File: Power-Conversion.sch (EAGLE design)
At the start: 46 parts, among them Q1 SUM90P10-19L, U7 LM2678

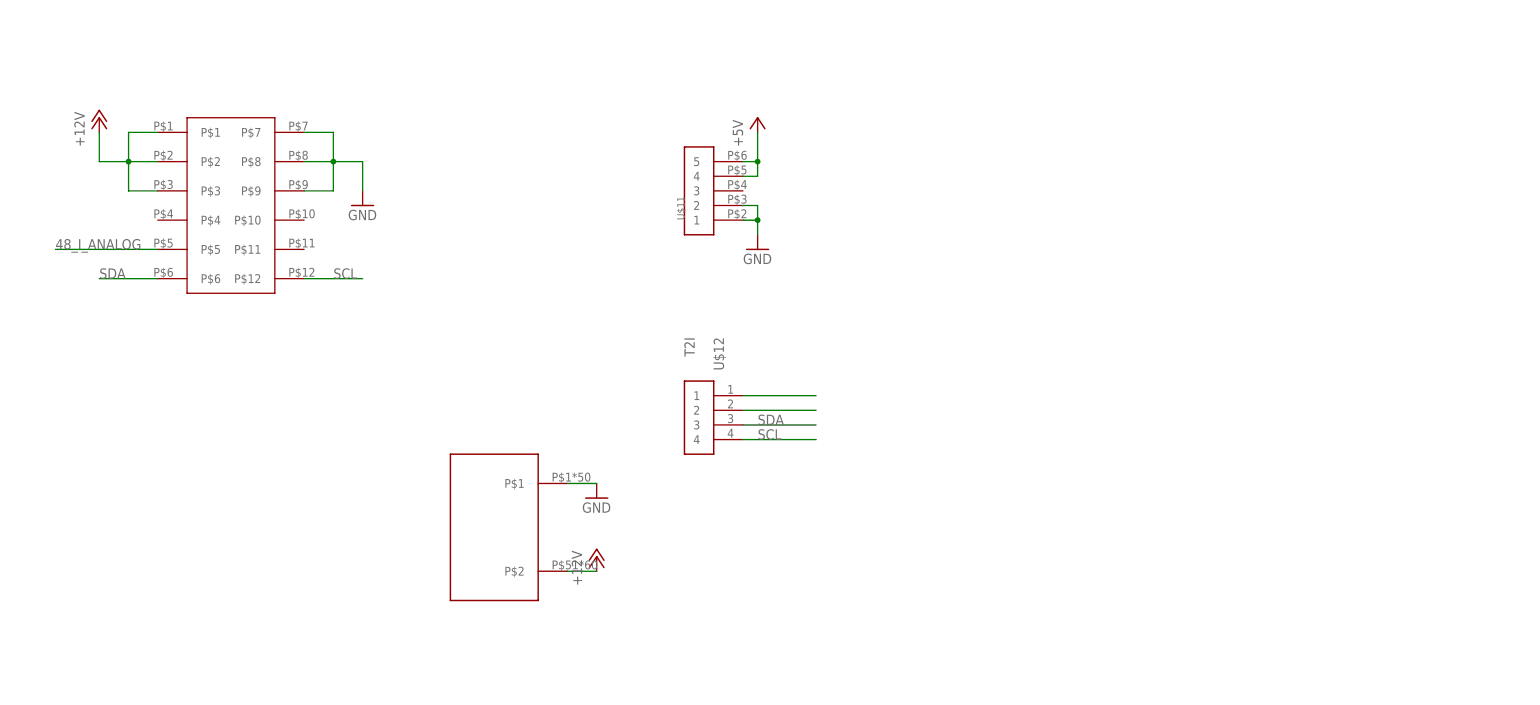
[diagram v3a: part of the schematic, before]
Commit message: Added new ESC to power distribution board part
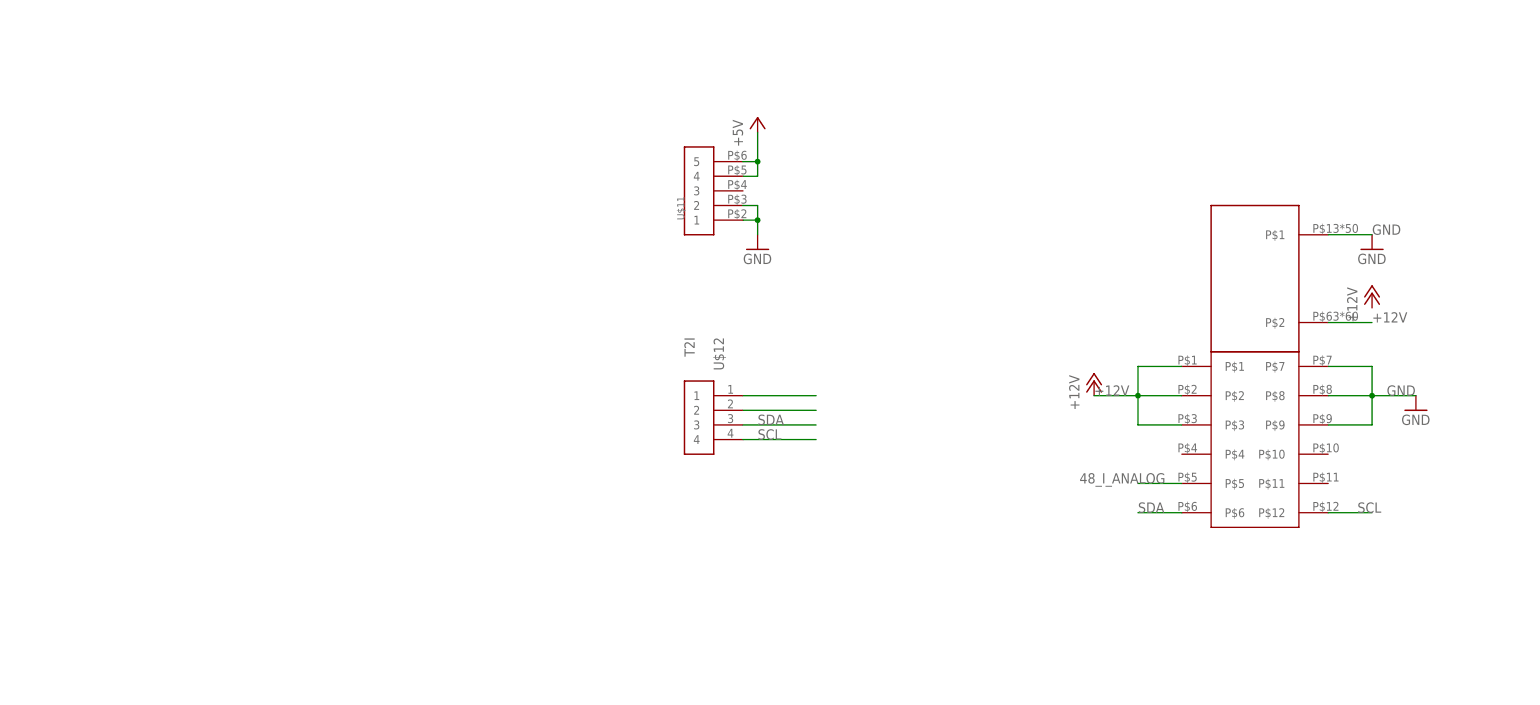
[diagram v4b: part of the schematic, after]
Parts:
- removed U$16: POWER_BRICK_CONNECTORS(2X6), MotherBoardParts2:POWER_BRICK_CONNECTORS(2X6)
- removed U$17: ESC-CONNECTORPARALLELL, MotherboardParts:ESC-CONNECTORPARALLELL
- added U$3: ESC-FULL, MotherboardParts:ESC-FULL
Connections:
- net +12V: now also U$3G$1.P$2, U$3G$2.P$1, U$3G$2.P$2, U$3G$2.P$3; no longer U$16.P$1, U$16.P$2, U$16.P$3, U$17.P$2
- net 48_I_ANALOG: now also U$3G$2.P$5; no longer U$16.P$5
- net GND: now also U$3G$1.P$1, U$3G$2.P$7, U$3G$2.P$8, U$3G$2.P$9; no longer U$16.P$7, U$16.P$8, U$16.P$9, U$17.P$1
- net SCL: now also U$3G$2.P$12; no longer U$16.P$12
- net SDA: now also U$3G$2.P$6; no longer U$16.P$6
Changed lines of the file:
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@@
 <?xml version="1.0" encoding="utf-8"?>
 <!DOCTYPE eagle SYSTEM "eagle.dtd">
-<eagle version="8.3.2">
+<eagle version="8.5.0">
 <drawing>
 <settings>
@@
 <part name="J1" library="SparkFun-Connectors" deviceset="BANANA_CONN" device=""/>
 <part name="J2" library="SparkFun-Connectors" deviceset="BANANA_CONN" device=""/>
-<part name="U$16" library="MotherBoardParts2" deviceset="POWER_BRICK_CONNECTORS(2X6)" device=""/>
 <part name="GND6" library="supply1" deviceset="GND" device=""/>
 <part name="U$2" library="diode" deviceset="DIODE" device=""/>
@@
 <part name="F7" library="PowerComponents" deviceset="PTC(2920L)" device="" value="10A"/>
 <part name="P+18" library="supply1" deviceset="+12V" device=""/>
-<part name="U$17" library="MotherboardParts" deviceset="ESC-CONNECTOR" device="PARALLELL" value="ESC-CONNECTORPARALLELL"/>
+<part name="U$3" library="MotherboardParts" deviceset="ESC-FULL" device=""/>
 </parts>
 <sheets>
@@
 <instance part="J1" gate="G$1" x="33.02" y="104.14"/>
 <instance part="J2" gate="G$1" x="33.02" y="99.06"/>
-<instance part="U$16" gate="G$1" x="50.8" y="378.46"/>
-<instance part="GND6" gate="1" x="73.66" y="373.38"/>
+<instance part="GND6" gate="1" x="248.92" y="365.76"/>
 <instance part="U$2" gate="G$1" x="53.34" y="447.04"/>
 <instance part="U$18" gate="G$1" x="142.24" y="441.96"/>
 <instance part="U$19" gate="G$1" x="233.68" y="441.96"/>
-<instance part="GND5" gate="1" x="114.3" y="322.58"/>
+<instance part="GND5" gate="1" x="256.54" y="337.82"/>
 <instance part="U$20" gate="G$1" x="50.8" y="482.6"/>
 <instance part="U$21" gate="G$1" x="139.7" y="482.6"/>
@@
 <instance part="P+9" gate="1" x="233.68" y="462.28"/>
 <instance part="P+13" gate="1" x="320.04" y="462.28"/>
-<instance part="P+14" gate="1" x="27.94" y="388.62"/>
-<instance part="P+15" gate="1" x="114.3" y="312.42"/>
+<instance part="P+14" gate="1" x="200.66" y="342.9"/>
+<instance part="P+15" gate="1" x="248.92" y="358.14"/>
 <instance part="R15" gate="G$1" x="187.96" y="520.7" rot="R180"/>
 <instance part="R5" gate="G$1" x="187.96" y="510.54" rot="R180"/>
@@
 <instance part="F7" gate="G$1" x="246.38" y="238.76" rot="MR90"/>
 <instance part="P+18" gate="1" x="246.38" y="251.46"/>
-<instance part="U$17" gate="G$1" x="96.52" y="317.5"/>
+<instance part="U$3" gate="G$1" x="228.6" y="360.68"/>
+<instance part="U$3" gate="G$2" x="226.06" y="327.66"/>
 </instances>
 <busses>
@@
 </segment>
 <segment>
-<pinref part="U$16" gate="G$1" pin="P$7"/>
-<wire x1="63.5" y1="386.08" x2="68.58" y2="386.08" width="0.1524" layer="91"/>
-<wire x1="68.58" y1="386.08" x2="68.58" y2="381" width="0.1524" layer="91"/>
-<pinref part="U$16" gate="G$1" pin="P$8"/>
-<wire x1="68.58" y1="381" x2="63.5" y2="381" width="0.1524" layer="91"/>
-<pinref part="U$16" gate="G$1" pin="P$9"/>
-<wire x1="63.5" y1="375.92" x2="68.58" y2="375.92" width="0.1524" layer="91"/>
-<wire x1="68.58" y1="375.92" x2="68.58" y2="381" width="0.1524" layer="91"/>
-<junction x="68.58" y="381"/>
-<wire x1="68.58" y1="381" x2="73.66" y2="381" width="0.1524" layer="91"/>
-<wire x1="73.66" y1="381" x2="73.66" y2="375.92" width="0.1524" layer="91"/>
-<pinref part="GND6" gate="1" pin="GND"/>
-</segment>
-<segment>
 <pinref part="U$20" gate="G$1" pin="D_GND"/>
 <wire x1="68.58" y1="472.44" x2="73.66" y2="472.44" width="0.1524" layer="91"/>
@@
 </segment>
 <segment>
-<pinref part="U$17" gate="G$1" pin="P$1"/>
-<wire x1="109.22" y1="325.12" x2="114.3" y2="325.12" width="0.1524" layer="91"/>
+<pinref part="U$3" gate="G$1" pin="P$1"/>
+<wire x1="241.3" y1="368.3" x2="248.92" y2="368.3" width="0.1524" layer="91"/>
+<label x="248.92" y="368.3" size="1.778" layer="95"/>
+<pinref part="GND6" gate="1" pin="GND"/>
+</segment>
+<segment>
+<pinref part="U$3" gate="G$2" pin="P$7"/>
+<wire x1="241.3" y1="345.44" x2="248.92" y2="345.44" width="0.1524" layer="91"/>
+<pinref part="U$3" gate="G$2" pin="P$9"/>
+<wire x1="241.3" y1="335.28" x2="248.92" y2="335.28" width="0.1524" layer="91"/>
+<wire x1="248.92" y1="345.44" x2="248.92" y2="340.36" width="0.1524" layer="91"/>
+<pinref part="U$3" gate="G$2" pin="P$8"/>
+<wire x1="248.92" y1="340.36" x2="248.92" y2="335.28" width="0.1524" layer="91"/>
+<wire x1="241.3" y1="340.36" x2="248.92" y2="340.36" width="0.1524" layer="91"/>
+<junction x="248.92" y="340.36"/>
+<wire x1="248.92" y1="340.36" x2="256.54" y2="340.36" width="0.1524" layer="91"/>
+<label x="251.46" y="340.36" size="1.778" layer="95"/>
 <pinref part="GND5" gate="1" pin="GND"/>
 </segment>
@@
 </segment>
 <segment>
-<pinref part="U$16" gate="G$1" pin="P$1"/>
-<wire x1="38.1" y1="386.08" x2="33.02" y2="386.08" width="0.1524" layer="91"/>
-<pinref part="U$16" gate="G$1" pin="P$2"/>
-<wire x1="33.02" y1="386.08" x2="33.02" y2="381" width="0.1524" layer="91"/>
-<wire x1="33.02" y1="381" x2="38.1" y2="381" width="0.1524" layer="91"/>
-<pinref part="U$16" gate="G$1" pin="P$3"/>
-<wire x1="38.1" y1="375.92" x2="33.02" y2="375.92" width="0.1524" layer="91"/>
-<wire x1="33.02" y1="375.92" x2="33.02" y2="381" width="0.1524" layer="91"/>
-<junction x="33.02" y="381"/>
-<wire x1="33.02" y1="381" x2="27.94" y2="381" width="0.1524" layer="91"/>
-<wire x1="27.94" y1="381" x2="27.94" y2="386.08" width="0.1524" layer="91"/>
-<pinref part="P+14" gate="1" pin="+12V"/>
-</segment>
-<segment>
 <pinref part="F7" gate="G$1" pin="2"/>
 <pinref part="P+18" gate="1" pin="+12V"/>
@@
 </segment>
 <segment>
-<pinref part="U$17" gate="G$1" pin="P$2"/>
-<wire x1="109.22" y1="309.88" x2="114.3" y2="309.88" width="0.1524" layer="91"/>
-<pinref part="P+15" gate="1" pin="+12V"/>
+<pinref part="U$3" gate="G$1" pin="P$2"/>
+<wire x1="241.3" y1="353.06" x2="248.92" y2="353.06" width="0.1524" layer="91"/>
+<label x="248.92" y="353.06" size="1.778" layer="95"/>
+</segment>
+<segment>
+<pinref part="U$3" gate="G$2" pin="P$1"/>
+<wire x1="215.9" y1="345.44" x2="208.28" y2="345.44" width="0.1524" layer="91"/>
+<pinref part="U$3" gate="G$2" pin="P$3"/>
+<wire x1="215.9" y1="335.28" x2="208.28" y2="335.28" width="0.1524" layer="91"/>
+<wire x1="208.28" y1="345.44" x2="208.28" y2="340.36" width="0.1524" layer="91"/>
+<pinref part="U$3" gate="G$2" pin="P$2"/>
+<wire x1="208.28" y1="340.36" x2="208.28" y2="335.28" width="0.1524" layer="91"/>
+<wire x1="215.9" y1="340.36" x2="208.28" y2="340.36" width="0.1524" layer="91"/>
+<junction x="208.28" y="340.36"/>
+<wire x1="208.28" y1="340.36" x2="200.66" y2="340.36" width="0.1524" layer="91"/>
+<label x="200.66" y="340.36" size="1.778" layer="95"/>
+<pinref part="P+14" gate="1" pin="+12V"/>
 </segment>
 </net>
@@
 <net name="SCL" class="0">
 <segment>
-<pinref part="U$16" gate="G$1" pin="P$12"/>
-<wire x1="63.5" y1="360.68" x2="73.66" y2="360.68" width="0.1524" layer="91"/>
-<label x="68.58" y="360.68" size="1.778" layer="95"/>
-</segment>
-<segment>
 <pinref part="R5" gate="G$1" pin="2"/>
 <wire x1="182.88" y1="510.54" x2="177.8" y2="510.54" width="0.1524" layer="91"/>
@@
 <label x="142.24" y="332.74" size="1.778" layer="95"/>
 </segment>
+<segment>
+<pinref part="U$3" gate="G$2" pin="P$12"/>
+<wire x1="241.3" y1="320.04" x2="248.92" y2="320.04" width="0.1524" layer="91"/>
+<label x="246.38" y="320.04" size="1.778" layer="95"/>
+</segment>
 </net>
 <net name="SDA" class="0">
-<segment>
-<pinref part="U$16" gate="G$1" pin="P$6"/>
-<wire x1="38.1" y1="360.68" x2="27.94" y2="360.68" width="0.1524" layer="91"/>
-<label x="27.94" y="360.68" size="1.778" layer="95"/>
-</segment>
 <segment>
 <pinref part="R15" gate="G$1" pin="2"/>
@@
 <wire x1="139.7" y1="335.28" x2="152.4" y2="335.28" width="0.1524" layer="91"/>
 <label x="142.24" y="335.28" size="1.778" layer="95"/>
+</segment>
+<segment>
+<pinref part="U$3" gate="G$2" pin="P$6"/>
+<wire x1="215.9" y1="320.04" x2="208.28" y2="320.04" width="0.1524" layer="91"/>
+<label x="208.28" y="320.04" size="1.778" layer="95"/>
 </segment>
 </net>
@@
 </segment>
 <segment>
-<pinref part="U$16" gate="G$1" pin="P$5"/>
-<wire x1="38.1" y1="365.76" x2="20.32" y2="365.76" width="0.1524" layer="91"/>
-<label x="20.32" y="365.76" size="1.778" layer="95"/>
-</segment>
-</net>
+<pinref part="U$3" gate="G$2" pin="P$5"/>
+<wire x1="215.9" y1="325.12" x2="208.28" y2="325.12" width="0.1524" layer="91"/>
+<label x="198.12" y="325.12" size="1.778" layer="95"/>
+</segment>
+</net>
